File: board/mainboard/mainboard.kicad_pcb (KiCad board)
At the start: 2 copper layers, 147.5 x 50 mm, 72 parts, among them P1 I2C, P10 BUMPERS, P12 POWER, P2 Motor1, P3 Motor2, P4 SPI, P6 CONN_5, P7 ANALOG, P8 OPTIONAL_PERIPH, P9 GPIO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

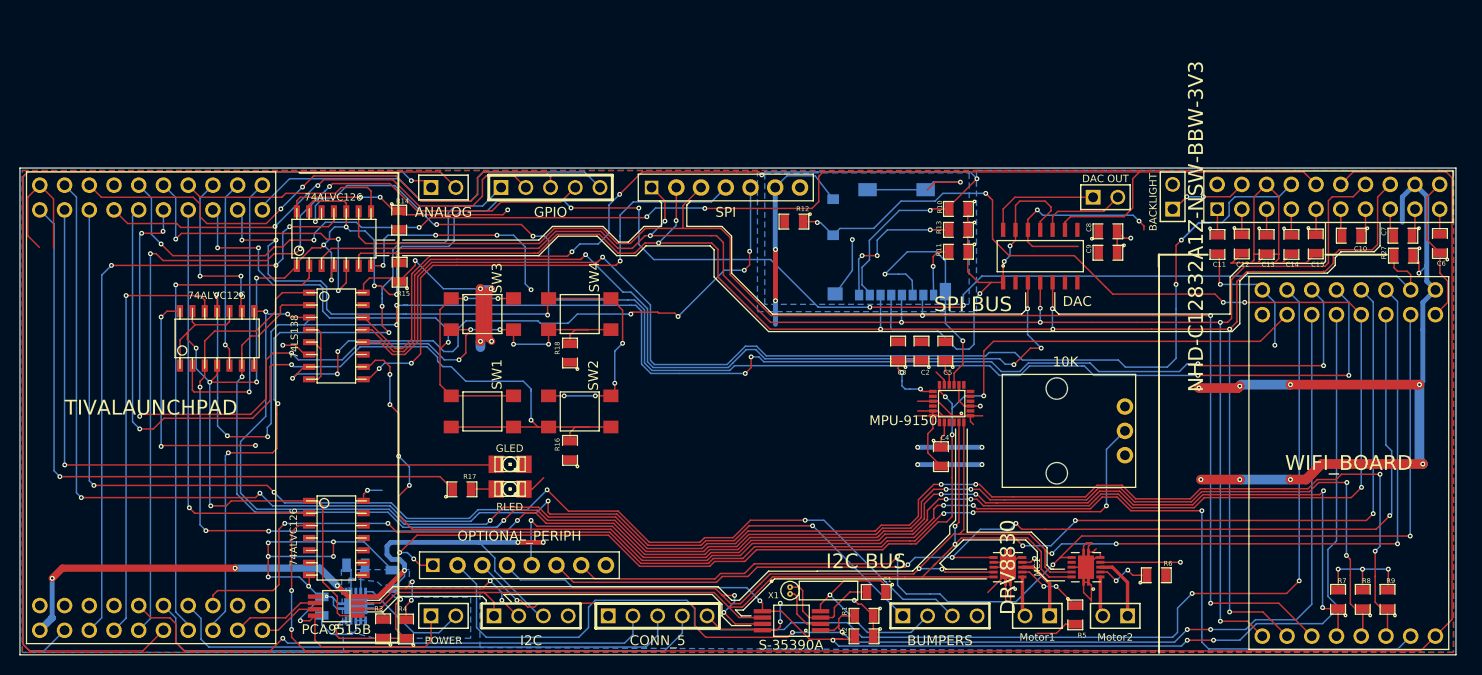
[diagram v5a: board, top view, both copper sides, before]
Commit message: Various changes
* Began Rev2 Layout
* Added Pullup Resistors to LP I2C
* Added IrDA Module
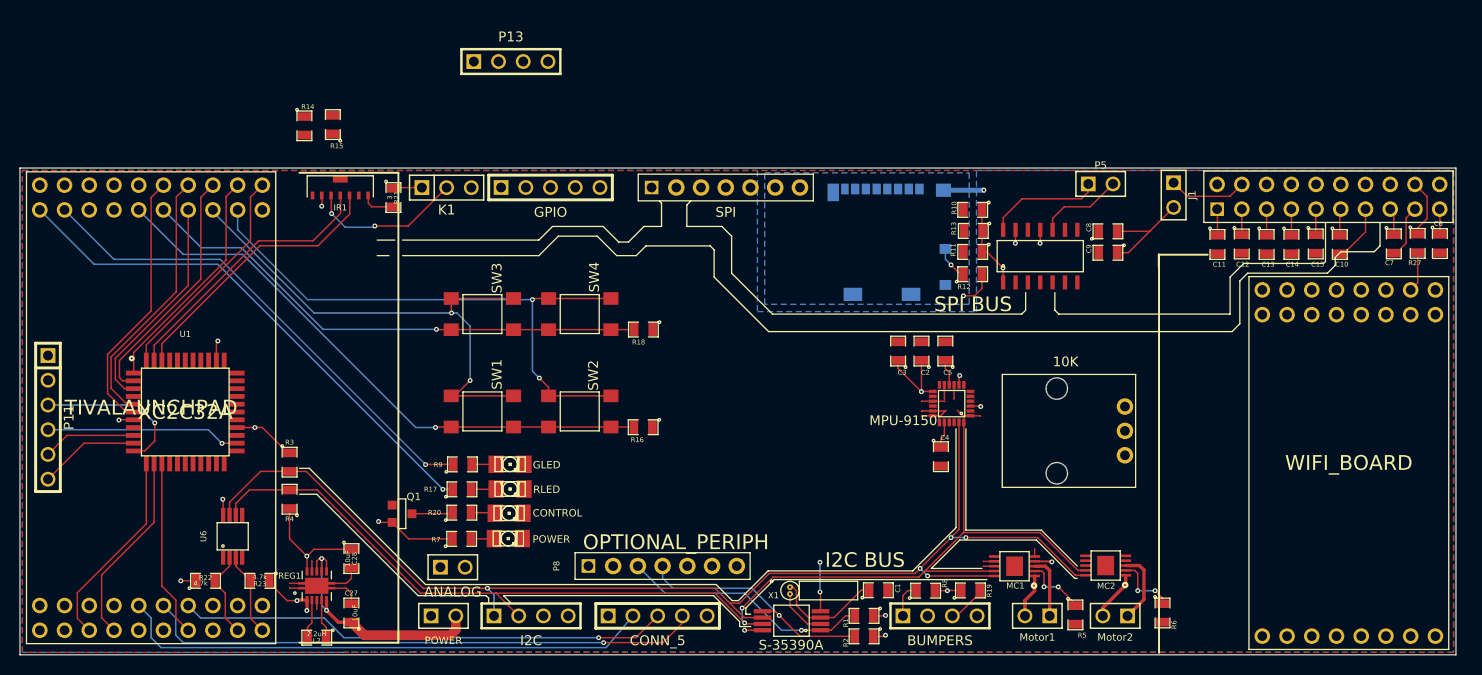
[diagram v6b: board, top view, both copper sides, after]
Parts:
- removed BACKLIGHT: BACKL, PIN_ARRAY_2X1
- removed DAC OUT: DAC, PIN_ARRAY_2X1
- removed U3, U4, U5: 74ALVC126, so-14
- added D3: POWER, LED-1206, F.Cu at (177.7, 148.1)
- added D4: CONTROL, LED-1206, F.Cu at (177.8, 145.5)
- added IR1: RPM841-H11, RPM973-H11, F.Cu at (160.4, 111.9)
- added J1: BACKL, PIN_ARRAY_2X1, F.Cu at (246.0, 112.8)
- added K1: IRDA_EN, PIN_ARRAY_3X1, F.Cu at (171.3, 112.0)
- added P11: CPLD_JTAG, PIN_ARRAY-6X1, F.Cu at (130.4, 135.6)
- added P13: UART, PIN_ARRAY_4x1, F.Cu at (177.9, 99.1)
- added P5: DAC, PIN_ARRAY_2X1, F.Cu at (238.5, 111.6)
- added Q1: BSS84, SOT23GDS, F.Cu at (166.8, 145.5)
- added R19: 47k, SM0805, F.Cu at (225.1, 153.4)
- added R20: 220, SM0805, F.Cu at (172.9, 145.4)
- added R21: 3, SM0805, F.Cu at (165.9, 113.0)
- added R22: 4.7k, SM0805, F.Cu at (146.6, 152.4)
- added R23: 4.7k, SM0805, F.Cu at (152.1, 152.4)
- C27, C28, L2, REG1: moved to F.Cu
- MC1, MC2: footprint DRV8830 -> DRV8830MSOP
- P8: footprint 1x8_Headers -> 1x7_Headers
- R10, R11, R13, R14, R15: value 50k -> 47k
- R17: value 560 -> 220
- R27: value 47K -> 10K
- R7, R9: value 47k -> 220
- U1: value 74LS138 -> XC2C32A; footprint so-16 -> CoolrunnerII
- moved R9 96.0 mm to (172.9, 140.4), turned to 0 degrees
- moved R7 90.2 mm to (172.9, 148.1), turned to 0 degrees
- moved R8 44.9 mm to (220.5, 153.4), turned to 0 degrees
- moved P7 39.0 mm to (172.0, 151.0)
- moved R3 19.6 mm to (155.2, 140.2), turned to 270 degrees
- moved R12 19.1 mm to (225.4, 120.9), turned to 0 degrees
- moved R4 17.9 mm to (155.2, 144.0)
- moved U1 17.4 mm to (144.5, 135.1), turned to 0 degrees
- moved R15 16.6 mm to (159.6, 105.5)
- moved P8 14.7 mm to (193.5, 150.9)
- moved R14 13.7 mm to (156.7, 105.7)
- moved U6 12.8 mm to (149.4, 147.8), turned to 90 degrees
- moved L2 8.45 mm to (158.0, 158.2)
- moved R18 7.92 mm to (191.5, 126.6), turned to 180 degrees
- moved R16 7.88 mm to (191.5, 136.6), turned to 180 degrees
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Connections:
- C1 pad 1: GND -> N-000007
- C1 pad 2: N-000007 -> GND
- C10 pad 1: N-0000040 (its old number) -> N-0000043
- C10 pad 2: N-0000039 (its old number) -> N-0000048
- C6 pad 1: GND -> N-0000031
- C6 pad 2: N-0000028 (its old number) -> GND
- C7 pad 1: N-0000037 -> N-0000044
- C7 pad 2: N-0000042 -> N-0000047
- D1 pad 1: LED2 -> N-0000051
- GLCD1 pad 10: N-0000028 (its old number) -> N-0000031
- GLCD1 pad 6: N-0000039 (its old number) -> N-0000043
- GLCD1 pad 7: N-0000040 (its old number) -> N-0000048
- GLCD1 pad 8: N-0000042 -> N-0000044
- GLCD1 pad 9: N-0000037 -> N-0000047
- R7 pad 1: SPI_SEL0 -> 3V3
- R7 pad 2: GND -> N-0000067
- R8 pad 1: SPI_SEL1 -> BUMP1
- R8 pad 2: GND -> 3V3
- R9 pad 1: SPI_SEL2 -> LED2
- R9 pad 2: GND -> N-0000051
- U1 pad 1: SPI_SEL0 -> SPI_SEL1_LP
- U1 pad 10: SPI_CS5 -> CPLD_TMS
- U1 pad 11: (no net) -> CPLD_TCK
- U1 pad 12: SPI_CS3 -> UART_RX_LP
- U1 pad 13: SPI_CS2 -> UART_TX_LP
- U1 pad 14: SPI_CS1 -> SPI_SCK_LP
- U1 pad 16: 3V3 -> (no net)
- U1 pad 2: SPI_SEL1 -> SPI_SEL2_LP
- U1 pad 3: SPI_SEL2 -> GLCD_A0_LP
- U1 pad 5: GND -> SPI_MISO_LP
- U1 pad 6: 3V3 -> SPI_MOSI_LP
- U1 pad 7: SPI_CS7 -> 3V3
- U1 pad 8: GND -> (no net)
- U1 pad 9: SPI_CS6 -> CPLD_TDI
- U6 pad 6: I2C_CL -> I2C_DA
- U6 pad 7: I2C_DA -> I2C_CL
- WB1 pad 4: SPI_SEL0 -> SPI_SEL0_CC
- WB1 pad 5: SPI_SEL1 -> SPI_SEL1_CC
- WB1 pad 6: SPI_SEL2 -> SPI_SEL2_CC
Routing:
- net GND: track 345.9 -> 40.4 mm, vias 23 -> 4
- net 3V3: track 372.4 -> 91.7 mm, vias 44 -> 21
- net CC_CONTROL: track 234.8 -> 4.13 mm, vias 14 -> 0
- net GLCD_A0: track 191.6 -> 0.00 mm, vias 2 -> 0
- net SPI_MOSI: track 178.8 -> 0.00 mm, vias 7 -> 0
- net SD_SWITCH: track 182.4 -> 3.55 mm, vias 8 -> 1
- net SPI_SCK: track 176.8 -> 0.00 mm, vias 7 -> 0
- net SPI_SEL0: track 172.9 -> 0.00 mm, vias 8 -> 0
- net SPI_SEL2: track 170.7 -> 0.00 mm, vias 7 -> 0
- net SPI_SEL1: track 166.5 -> 0.00 mm, vias 6 -> 0
- net SPI_MISO: track 148.3 -> 0.00 mm, vias 3 -> 0
- net RST: track 144.9 -> 0.00 mm, vias 5 -> 0
- net SPI_CS5: track 144.1 -> 0.00 mm, vias 7 -> 0
- net SPI_CS3: track 134.4 -> 0.00 mm, vias 3 -> 0
- net UART_TX: track 161.2 -> 28.1 mm, vias 9 -> 0
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- removed copper zone on B.Cu, net N-00000115

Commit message: Further work on the rev2 layout
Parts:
- P6: value CONN_5 -> LINE SENSORS
- moved P7 74.3 mm to (235.1, 111.9)
- moved P13 51.8 mm to (176.8, 150.9)
- moved R16 23.3 mm to (168.4, 133.3), turned to 270 degrees
- moved R18 23.2 mm to (168.4, 127.8), turned to 90 degrees
- moved C2 5.01 mm to (218.7, 133.6), turned to 270 degrees
- moved C3 4.91 mm to (216.7, 133.6), turned to 270 degrees
- moved DAC1 4.17 mm to (236.5, 119.0)
- moved C9 4.02 mm to (242.7, 120.8), turned to 270 degrees
- moved D2 3.56 mm to (177.8, 139.4)
- moved D4 3.56 mm to (177.8, 141.9)
- moved R17 3.56 mm to (172.9, 139.4)
- moved R20 3.56 mm to (172.9, 141.8)
- moved R7 3.56 mm to (172.9, 144.5)
- moved R9 3.56 mm to (172.9, 136.9)
- moved D1 3.56 mm to (177.8, 136.9)
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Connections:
- U1 pad 27: SPI_SCK -> SPI_SEL0_CC
- U1 pad 28: SPI_MOSI -> SPI_SEL1_CC
- U1 pad 29: SPI_MISO -> SPI_SEL2_CC
- U1 pad 30: SPI_SEL0_CC -> CC_CONTROL
- U1 pad 31: SPI_SEL1_CC -> SPI_MISO
- U1 pad 32: SPI_SEL2_CC -> SPI_MOSI
- U1 pad 33: CC_CONTROL -> SPI_SCK
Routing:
- net SPI_MOSI: track 0.00 -> 205.6 mm, vias 0 -> 7
- net SPI_SCK: track 0.00 -> 197.7 mm, vias 0 -> 7
- net SPI_MISO: track 0.00 -> 172.3 mm, vias 0 -> 5
- net SPI_CS5: track 0.00 -> 153.4 mm, vias 0 -> 4
- net UART_RX: track 28.4 -> 178.3 mm, vias 0 -> 3
- net UART_TX: track 28.1 -> 176.3 mm, vias 0 -> 3
- net SPI_CS3: track 0.00 -> 136.1 mm, vias 0 -> 5
- net SPI_SEL2_CC: track 0.00 -> 127.9 mm, vias 0 -> 1
- net SPI_SEL1_CC: track 0.00 -> 125.0 mm, vias 0 -> 1
- net SPI_SEL0_CC: track 0.00 -> 122.2 mm, vias 0 -> 1
- net SPI_CS1: track 0.00 -> 111.9 mm, vias 0 -> 5
- net 3V3: track 91.7 -> 200.4 mm, vias 21 -> 35
- net SPI_CS2: track 0.00 -> 104.7 mm, vias 0 -> 4
- net MOTOR1F: track 0.00 -> 95.1 mm, vias 0 -> 3
- net MOTOR2F: track 0.00 -> 86.8 mm, vias 0 -> 1
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
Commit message: Finished draft 1 of Rev 2 layout
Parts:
- removed R10: 47k, SM0805
- added AUD1: LM4808, LM4808, F.Cu at (207.4, 120.0)
- added C16: 1uF, SM0805, F.Cu at (133.9, 144.4)
- added C17: 0.47uF, SM0805, F.Cu at (196.3, 130.9)
- added C18: 680nF, SM0805, F.Cu at (198.5, 135.0)
- added C19: 680nF, SM0805, F.Cu at (192.2, 140.2)
- added C20: 2.2nF, SM0805, F.Cu at (194.2, 140.2)
- added C21: 2.2uF, SM0805, F.Cu at (224.3, 120.1)
- added C22: 2.2uF, SM0805, F.Cu at (224.3, 116.2)
- added C23: 1uF, SM0805, F.Cu at (210.1, 113.2)
- added C24: 1uF, SM0805, F.Cu at (198.4, 130.9)
- added C25: 0.1uF, SM0805, F.Cu at (203.6, 119.9)
- added C26: 100uF, SM0805, F.Cu at (220.6, 118.6)
- added C29: 100uF, SM0805, F.Cu at (213.2, 118.9)
- added HP1: HP_JACK, HeadphoneJack, F.Cu at (216.9, 118.1)
- added MIC1: CMA-4544PF-W, CMA-4544, F.Cu at (205.1, 134.9)
- added P14: AUDIO, PIN_ARRAY_2X1, F.Cu at (229.1, 111.9)
- added P15: MIC, PIN_ARRAY_2X1, F.Cu at (198.1, 140.5)
- added R24: 2.2k, SM0805, F.Cu at (194.3, 130.9)
- added R25: 100k, SM0805, F.Cu at (207.4, 115.2)
- added R26: 100k, SM0805, F.Cu at (208.7, 123.7)
- added R28: 3.9k, SM0805, F.Cu at (226.9, 122.9)
- added R29: 3.9k, SM0805, F.Cu at (224.3, 112.5)
- added R30: 3.9k, SM0805, F.Cu at (220.6, 122.2)
- added R31: 3.9k, SM0805, F.Cu at (212.2, 116.1)
- added R32: 150k, SM0805, F.Cu at (192.3, 134.7)
- added R33: 150k, SM0805, F.Cu at (192.3, 130.9)
- added U2: TLV702, SOT23-5, F.Cu at (135.1, 147.7)
- added U3: MAX9814, MAX9814, F.Cu at (195.6, 135.6)
- P6: value LINE SENSORS -> CONN_5
- R11, R12, R13: moved to B.Cu
- moved R14 44.0 mm to (195.7, 126.0), turned to 90 degrees
- moved R15 39.6 mm to (193.5, 126.0)
- moved R11 21.8 mm to (203.6, 117.2), turned to 0 degrees
- moved C2 7.11 mm to (224.9, 130.2), turned to 0 degrees
- moved R12 5.50 mm to (224.7, 115.4), turned to 90 degrees
- moved C3 2.47 mm to (219.1, 134.1)
- moved R13 1.91 mm to (226.8, 115.4), turned to 90 degrees
- moved C4 1.60 mm to (221.5, 138.2), turned to 180 degrees
- moved X1 1.11 mm to (205.5, 153.4)
- moved RV1 0.98 mm to (234.9, 136.8)
- moved C5 0.90 mm to (221.1, 130.2)
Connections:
- P13 pad 1: 3V3 -> UART_TX
- P13 pad 3: UART_TX -> 3V3
- U1 pad 15: (no net) -> +1.8V
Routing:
- net GND: track 56.3 -> 385.9 mm, vias 6 -> 36
- net 3V3: track 200.4 -> 391.6 mm, vias 35 -> 51
- net CC_CONTROL: track 23.2 -> 170.1 mm, vias 0 -> 5
- net AIN1: track 0.00 -> 133.4 mm, vias 0 -> 5
- net RST: track 24.0 -> 155.1 mm, vias 2 -> 10
- net AIN2: track 0.00 -> 130.9 mm, vias 0 -> 6
- net GLCD_A0: track 54.9 -> 182.2 mm, vias 0 -> 5
- net BUMP2: track 4.04 -> 114.5 mm, vias 0 -> 5
- net BUMP1: track 3.68 -> 113.5 mm, vias 0 -> 6
- net POT: track 0.00 -> 104.8 mm, vias 0 -> 5
- net PA5: track 0.00 -> 72.4 mm, vias 0 -> 7
- net SD_SWITCH: track 86.5 -> 132.3 mm, vias 1 -> 0
- net N-00000129: track 0.00 -> 24.3 mm, vias 0 -> 2
- net N-00000133: track 0.00 -> 21.0 mm
- net I2C_CL: track 159.2 -> 177.9 mm
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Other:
- board text added: "Proxima Rev 2.0"
- board text removed: "Proxima Rev 1.2"
